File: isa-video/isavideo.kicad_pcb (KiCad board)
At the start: 4 copper layers, 106.4 x 95 mm, 142 parts, among them J1 PROG, J2 DB15_Female_HighDensity_Mount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, J3 PJRAN1X1U04X, J4 10029449-111RLF, J5 Conn_ISA_8bit, J6 RFMOD, J7 Conn_01x05, J8 Conn_02x06_Odd_Even, SW1 SW_DIP_x04, U1 ICE40HX4K-TQ144, U10 APX803S00-29SA-7, U11 74HCT125, U12 TFP410PAP, U2 SST26VF080A-104I/SN, U3 74ALVC164245, U4 74ALVC164245, U5 74ALVC164245, U6 ADA4891-3, U7 IS61WV5128BLL-10KLI, U8 LD1085D2T33R, U9 AP2114HA-1.2, X1 10MHz, X2 14.318MHz

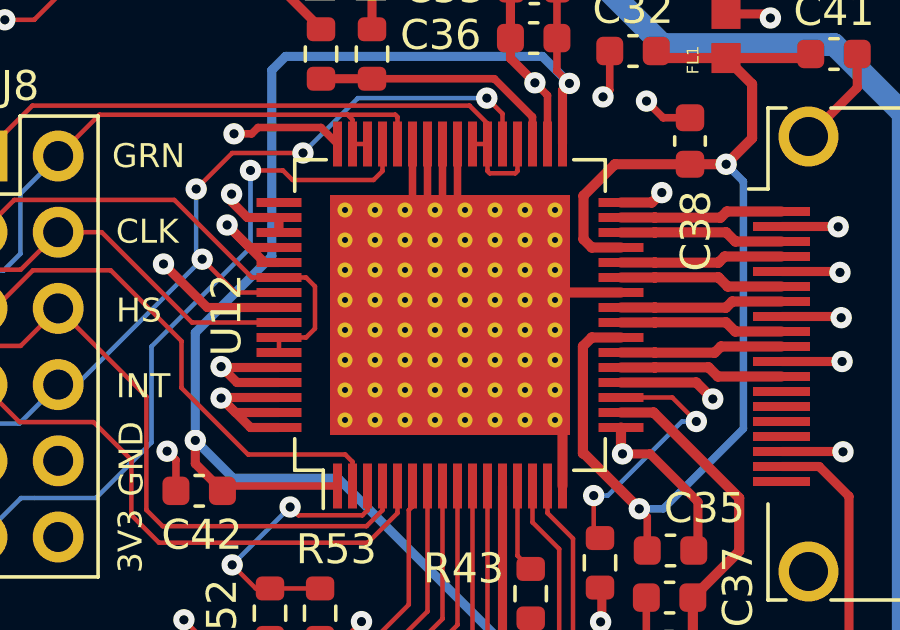
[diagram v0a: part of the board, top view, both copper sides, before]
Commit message: Adjust TFP410 vias
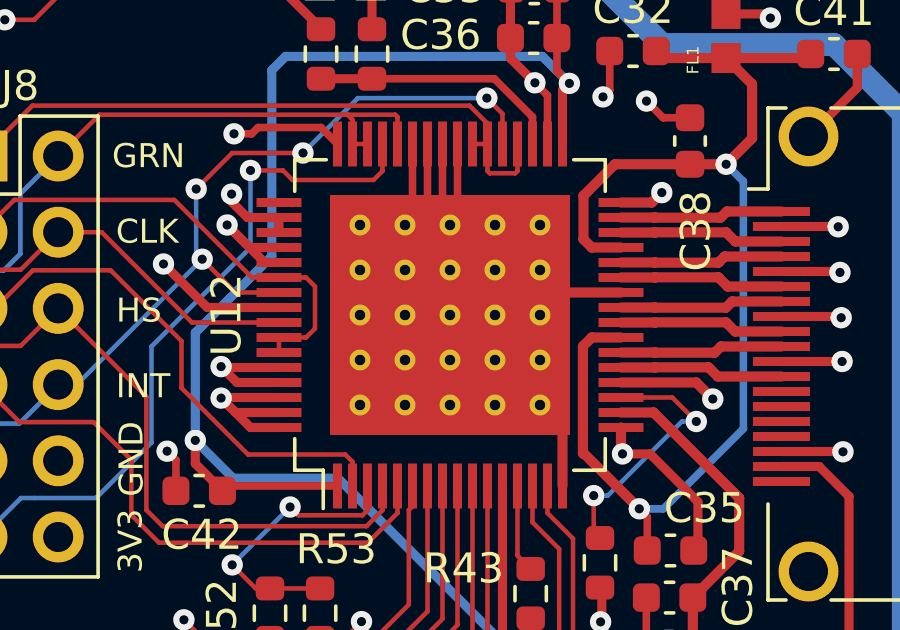
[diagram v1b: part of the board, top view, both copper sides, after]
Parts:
- U12: footprint Package_QFP:HTQFP-64-1EP_10x10mm_P0.5mm_EP8x8mm_Mask4.4x4.4mm_ThermalVias -> libraries:TFP410_ThermalVias

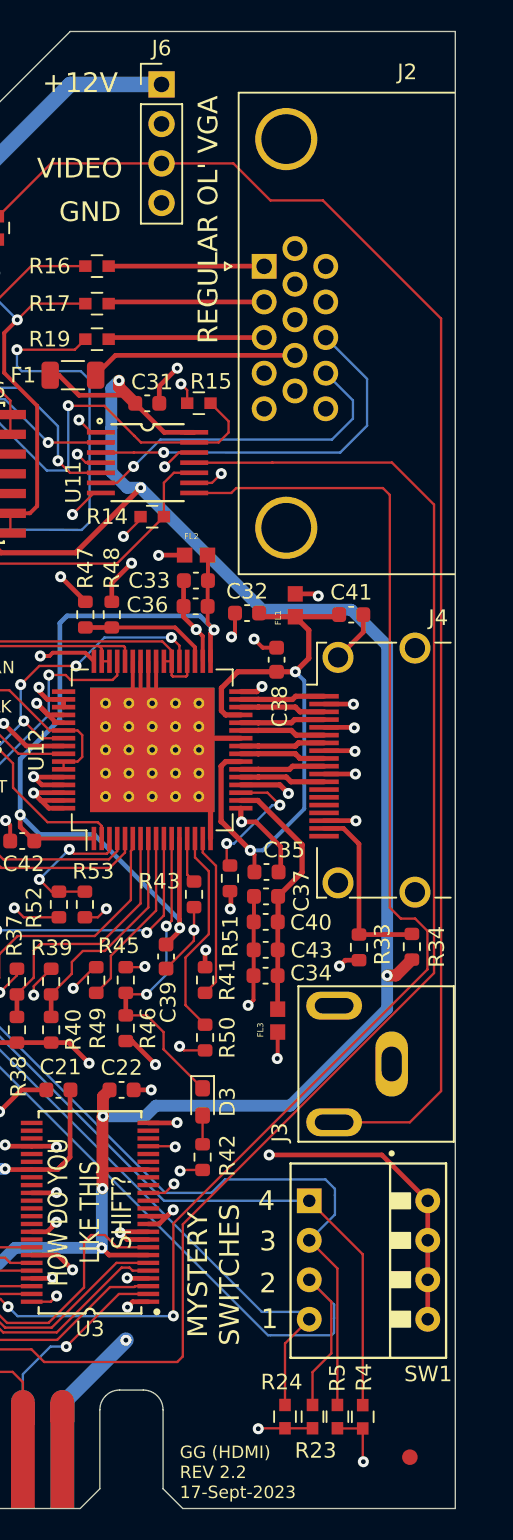
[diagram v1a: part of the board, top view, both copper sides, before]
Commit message: minor adjustment to VGA footprint
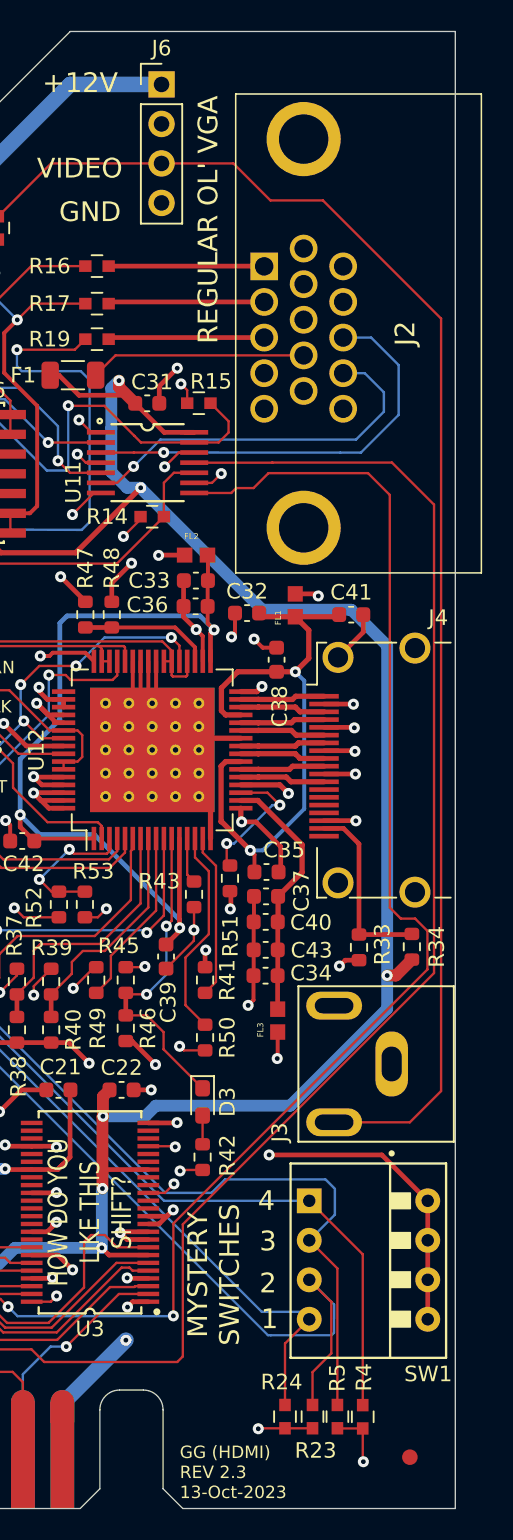
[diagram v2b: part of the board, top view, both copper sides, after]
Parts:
- J2: footprint Connector_Dsub:DSUB-15-HD_Female_Horizontal_P2.29x1.98mm_EdgePinOffset8.35mm_Housed_MountingHolesOffset10.89mm -> libraries:23117631
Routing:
- net GND: track 375.5 -> 368.3 mm
- net /VGA_HSYNC_5V: track 24.6 -> 27.7 mm
- net /VGA_VSYNC_5V: track 21.6 -> 24.5 mm
- net /Bus Interface/RDY_5V: track 112.8 -> 113.5 mm
- net Net-(F1-Pad1): track 13.3 -> 13.9 mm
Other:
- board text added: "GG (HDMI) REV 2.3 13-Oct-2023"
- board text removed: "GG (HDMI) REV 2.2 17-Sept-2023"
